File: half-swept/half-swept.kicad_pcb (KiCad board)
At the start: 2 copper layers, 109 x 87.4 mm, 24 parts, among them J2 AudioJack4dpb, SW1 SW_Push, SW10 SW_Push, SW11 SW_Push, SW12 SW_Push, SW13 SW_Push, SW14 SW_Push, SW15 SW_Push, SW16 SW_Push, SW17 SW_Push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

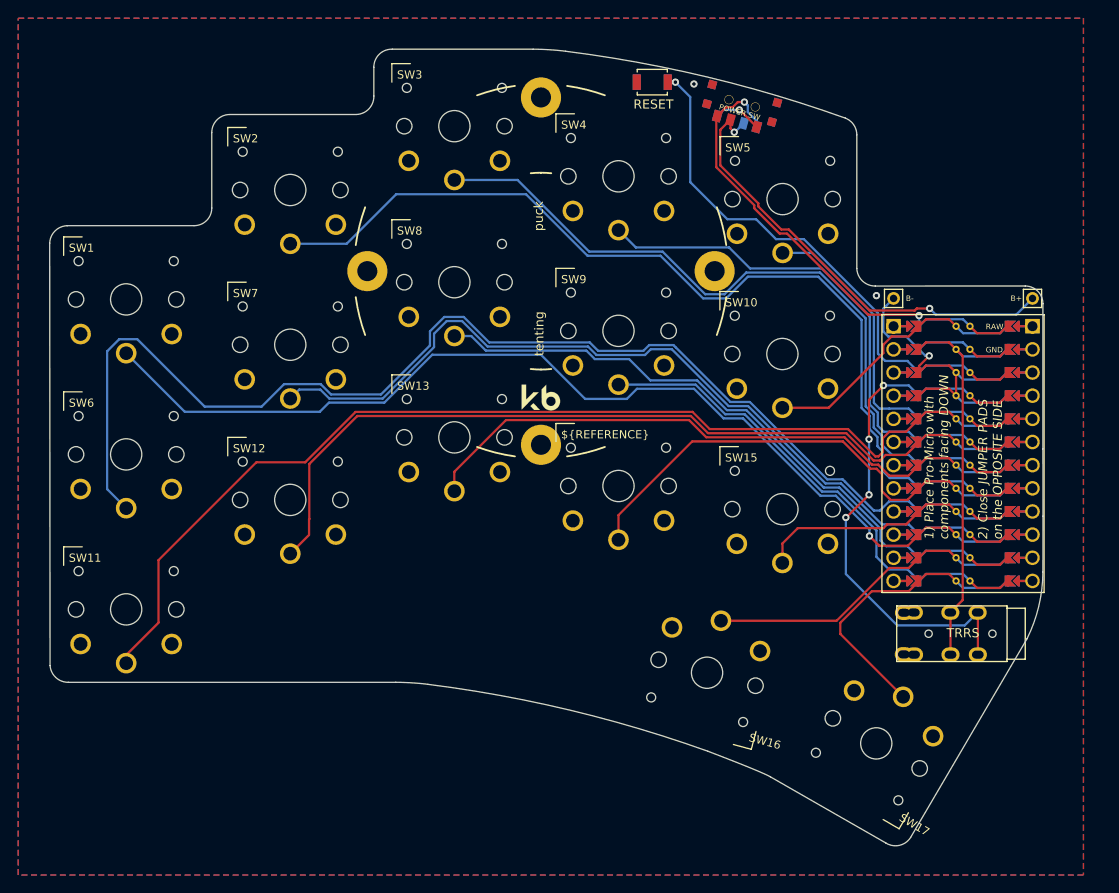
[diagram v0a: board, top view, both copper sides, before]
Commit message: chore: update traces, add footprint for silkscreen and mask, modify the edge cut
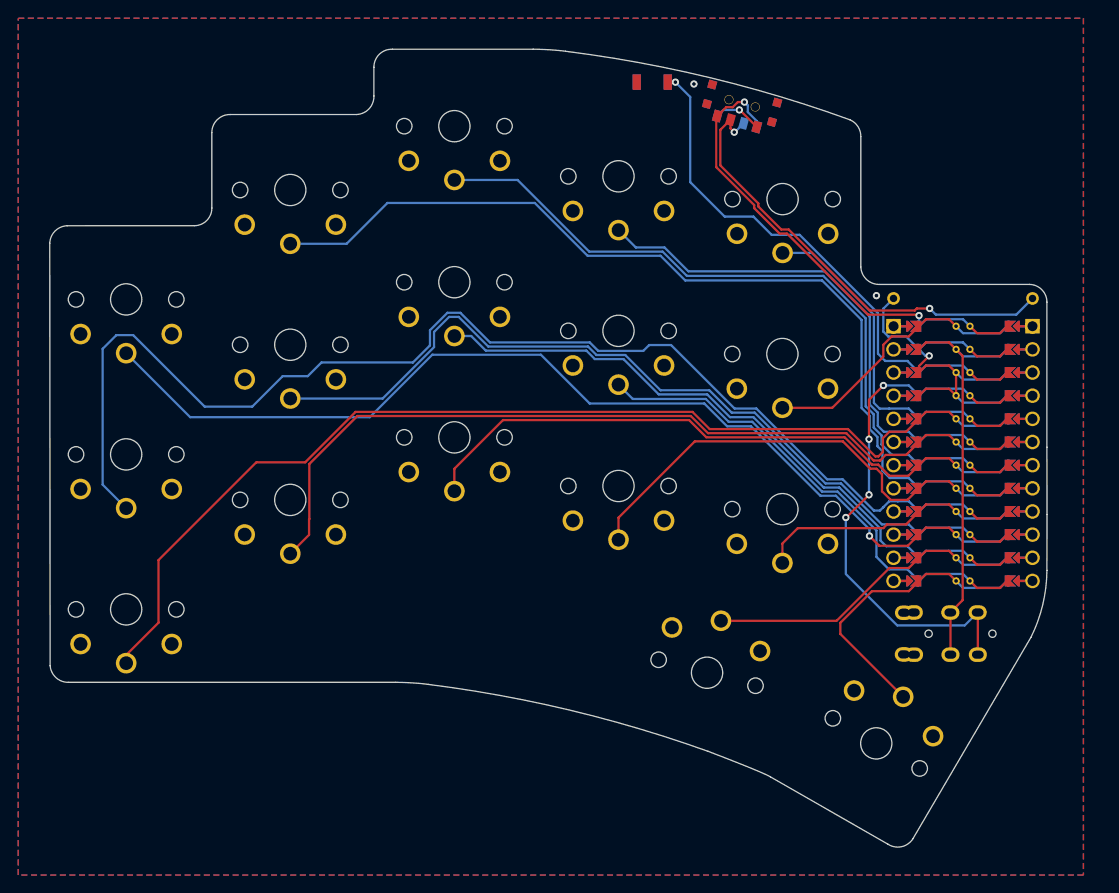
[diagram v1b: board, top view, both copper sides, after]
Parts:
- removed REF**: Tenting Puck, kbd:Tenting_Puck2
- added G***: LOGO, half-swept:moaki-ascii-mask, F.Cu at (53.5, 83.0)
- added G***: LOGO, half-swept:saadi-part-2, B.Cu at (71.5, 78.0)
- added G***: LOGO, half-swept:saadi-part-1, B.Cu at (54.0, 84.5)
- SW1, SW10, SW11, SW12, SW13, SW14, SW15, SW16, SW17, SW2, SW3, SW4, SW5, SW6, SW7, SW8, SW9: footprint * duckyb-collection:SW_PG1350_rev_DPB -> Library:SW_PG1350_rev_DPB
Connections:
- RSW2 pad 1: reset -> gnd
- RSW2 pad 2: reset -> gnd
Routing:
- net Switch2: track 94.9 -> 92.1 mm
- net Switch3: track 73.0 -> 71.0 mm
- net Switch7: track 84.4 -> 83.5 mm
- net Switch6: track 126.9 -> 127.6 mm
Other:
- board size 109 x 87.4 mm -> 109.4 x 87.5 mm
- board text removed: "${REFERENCE}"
- board text removed: "1) Place Pro-Micro with components facing DOWN"
- board text removed: "2) Close JUMPER PADS on the OPPOSITE SIDE"
- board text removed: "B+"
- board text removed: "B-"
- board text removed: "GND"
- board text removed: "RAW"
- board text removed: "TRRS"

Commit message: final -- add cool silkscreen, reduce errors and wardnings from kicad
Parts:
- removed the G*** at (71.5, 78.0)
- removed the G*** at (54.0, 84.5)
- added G***: LOGO, half-swept:owl, F.Cu at (83.0, 62.0)
- added G***: LOGO, LOGO, B.Cu at (51.0, 82.0)
- added G***: LOGO, LOGO, B.Cu at (70.5, 85.5)
- moved RSW2 0.05 mm to (84.8, 22.2)
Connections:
- RSW2 pad 1: gnd -> (no net)
- RSW2 pad 2: gnd -> (no net)
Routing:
- net Switch6: track 127.6 -> 128.7 mm
- net reset: track 49.7 -> 48.8 mm
- net gnd: track 15.1 -> 15.7 mm
